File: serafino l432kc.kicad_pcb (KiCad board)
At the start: 4 copper layers, 17.8 x 35.6 mm, 31 parts, among them J1 USB_B_Micro, J2 Conn_01x14, J3 Conn_01x14, Q1 AO3401A, SW1 SW_Push, U1 AP2112K-3.3, U2 USBLC6-2SC6, U3 STM32L432KCUx, Y1 32.768K

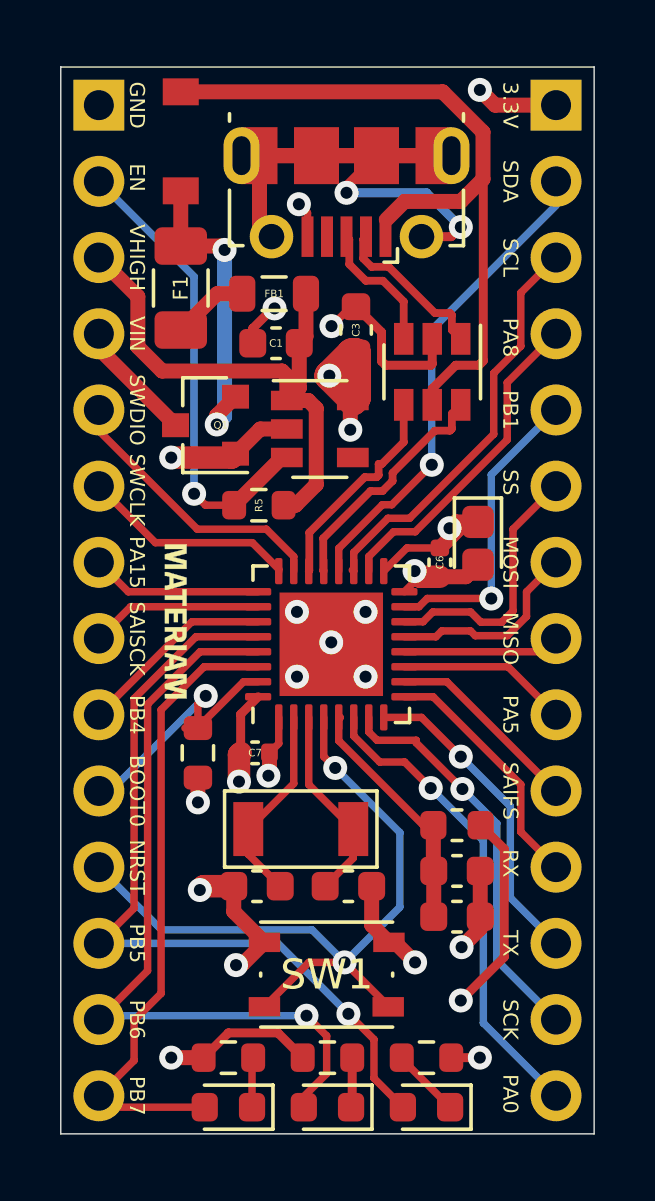
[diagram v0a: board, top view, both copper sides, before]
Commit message: Cambio de layout en leds
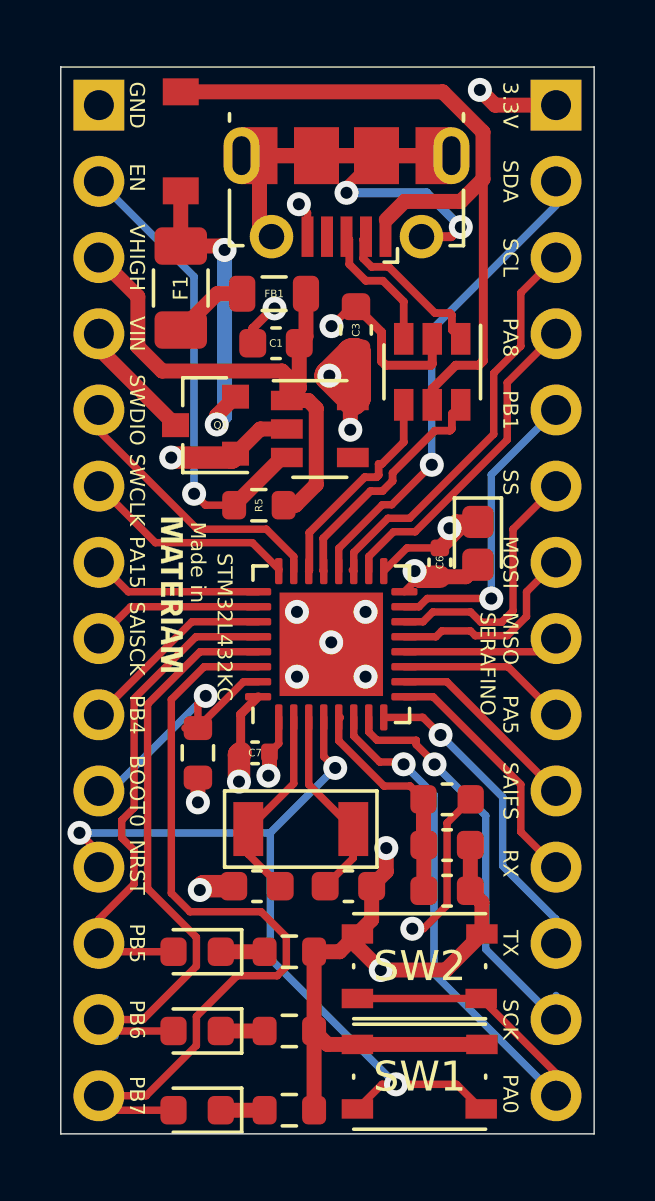
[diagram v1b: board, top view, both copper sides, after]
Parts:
- added SW2: SW_Push, Button_Switch_SMD:SW_Push_1P1T_NO_Vertical_Wuerth_434133025816, F.Cu at (199.4, 121.0)
- moved D1 9.24 mm to (192.0, 120.5)
- moved R1 5.78 mm to (195.1, 120.5)
- moved D3 5.03 mm to (192.0, 123.2)
- moved SW1 4.60 mm to (199.4, 124.7)
- moved R4 2.68 mm to (195.1, 125.8), turned to 0 degrees
- moved R3 1.55 mm to (195.1, 123.2), turned to 0 degrees
- moved D4 1.05 mm to (192.0, 125.8)
- moved C10 0.92 mm to (200.3, 117.0)
- moved C9 0.92 mm to (200.3, 118.5)
- moved L1 0.92 mm to (200.3, 115.5)
- moved G*** 0.90 mm to (191.1, 108.6)
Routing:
- net LED0: track 26.8 -> 16.5 mm, vias 1 -> 0
- net GND: track 36.3 -> 45.0 mm, vias 17 -> 14
- net PA0: track 15.9 -> 24.2 mm
- net LED2: track 21.2 -> 27.1 mm
- net LED1: track 26.3 -> 21.4 mm, vias 1 -> 0
- net NRST: track 24.9 -> 27.6 mm, vias 2 -> 3
- net +3V3: track 22.9 -> 21.5 mm
- net Net-(D1-Pad1): track 2.32 -> 1.46 mm
- net SPI1_SCK: track 13.4 -> 14.2 mm
- net +3.3VA: track 8.20 -> 7.52 mm
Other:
- board text added: "Made in"
- board text added: "SERAFINO"
- board text added: "STM32L432KC"

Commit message: BOM start
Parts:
- added G***: LOGO, serafino l432kc:cupid, F.Cu at (197.4, 104.8)
- moved G*** 0.07 mm to (191.2, 108.6)
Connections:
- R2 pad 1: +3V3 -> GND
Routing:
- net GND: track 45.0 -> 46.4 mm
- net +3V3: track 21.5 -> 20.7 mm, vias 7 -> 6
- net BOOT0: track 9.15 -> 8.51 mm
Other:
- board text added: "* Ultra-low-power * Arm ® Cortex ® M4 * 32-bit MCU+FPU@80Mhz * 256KB Flash * 64KB SRAM"
- board text added: "RST"
- board text added: "SERAFINO L432"
- board text added: "SW0"
- board text added: "http://materiam.com/serafino"
- board text removed: "SERAFINO"

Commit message: version acorde con primer prototipo
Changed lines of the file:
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@@
     (thickness 1.6)
     (drawings 41)
-    (tracks 374)
+    (tracks 377)
     (zones 0)
     (modules 33)
@@
   )
   (setup
-    (last_trace_width 0.25)
+    (last_trace_width 0.3)
     (user_trace_width 0.3)
     (user_trace_width 0.5)
@@
   (segment (start 200.6444 124.968) (end 201.4654 125.789) (width 0.25) (layer F.Cu) (net 3) (status 20))
   (segment (start 198.628 124.968) (end 200.6444 124.968) (width 0.25) (layer F.Cu) (net 3))
-  (segment (start 198.992 107.089) (end 200.0885 107.089) (width 0.25) (layer F.Cu) (net 4) (status 20))
-  (segment (start 198.219 107.862) (end 198.992 107.089) (width 0.25) (layer F.Cu) (net 4) (status 10))
   (segment (start 200.956 106.2215) (end 201.3585 106.2215) (width 0.5) (layer F.Cu) (net 4) (status 30))
   (segment (start 200.0885 107.089) (end 200.956 106.2215) (width 0.5) (layer F.Cu) (net 4) (status 30))
-  (segment (start 194.719 113.609) (end 194.409 113.919) (width 0.25) (layer F.Cu) (net 4) (status 20))
-  (segment (start 194.719 112.737) (end 194.719 113.609) (width 0.25) (layer F.Cu) (net 4) (status 10))
   (segment (start 197.188 100.7035) (end 197.2945 100.597) (width 0.5) (layer F.Cu) (net 4) (status 30))
   (segment (start 203.962 92.329) (end 203.454 92.329) (width 0.5) (layer F.Cu) (net 4) (status 30))
@@
   (segment (start 200.3298 118.994234) (end 199.541918 119.782116) (width 0.25) (layer F.Cu) (net 4))
   (segment (start 201.1173 115.4684) (end 200.3298 116.2559) (width 0.25) (layer F.Cu) (net 4) (status 10))
+  (segment (start 198.907304 107.089) (end 200.0885 107.089) (width 0.3) (layer F.Cu) (net 4))
+  (segment (start 198.219 107.777304) (end 198.907304 107.089) (width 0.3) (layer F.Cu) (net 4))
+  (segment (start 198.219 107.862) (end 198.219 107.777304) (width 0.3) (layer F.Cu) (net 4))
+  (segment (start 194.719 113.609) (end 194.409 113.919) (width 0.3) (layer F.Cu) (net 4))
+  (segment (start 194.719 112.737) (end 194.719 113.609) (width 0.3) (layer F.Cu) (net 4))
   (segment (start 195.219 114.943) (end 193.703 116.459) (width 0.25) (layer F.Cu) (net 5) (status 20))
   (segment (start 195.219 112.737) (end 195.219 114.943) (width 0.25) (layer F.Cu) (net 5) (status 10))
@@
   (segment (start 202.184 117.690002) (end 203.962 119.468002) (width 0.25) (layer B.Cu) (net 22) (status 20))
   (segment (start 202.184 115.395304) (end 202.184 117.690002) (width 0.25) (layer B.Cu) (net 22))
-  (segment (start 197.995988 113.49951) (end 199.30149 113.49951) (width 0.25) (layer F.Cu) (net 23))
-  (segment (start 197.719 113.222522) (end 197.995988 113.49951) (width 0.25) (layer F.Cu) (net 23))
   (segment (start 197.719 112.737) (end 197.719 113.222522) (width 0.25) (layer F.Cu) (net 23) (status 10))
   (via (at 199.911198 114.303214) (size 0.8) (drill 0.4) (layers F.Cu B.Cu) (net 23))
   (segment (start 199.883882 114.22888) (end 199.91578 114.22888) (width 0.25) (layer F.Cu) (net 23))
-  (segment (start 199.30149 113.646488) (end 199.883882 114.22888) (width 0.25) (layer F.Cu) (net 23))
-  (segment (start 199.30149 113.49951) (end 199.30149 113.646488) (width 0.25) (layer F.Cu) (net 23))
   (segment (start 203.962 122.008002) (end 203.962 122.809) (width 0.25) (layer B.Cu) (net 23) (status 30))
   (segment (start 201.618009 120.465009) (end 203.962 122.809) (width 0.25) (layer B.Cu) (net 23) (status 20))
   (segment (start 201.618009 116.010025) (end 201.618009 120.465009) (width 0.25) (layer B.Cu) (net 23))
   (segment (start 199.911198 114.303214) (end 201.618009 116.010025) (width 0.25) (layer B.Cu) (net 23))
+  (segment (start 199.182983 113.574999) (end 199.911198 114.303214) (width 0.25) (layer F.Cu) (net 23))
+  (segment (start 198.071477 113.574999) (end 199.182983 113.574999) (width 0.25) (layer F.Cu) (net 23))
+  (segment (start 197.76899 113.272512) (end 198.071477 113.574999) (width 0.25) (layer F.Cu) (net 23))
+  (segment (start 197.757478 113.222522) (end 197.76899 113.234034) (width 0.25) (layer F.Cu) (net 23))
+  (segment (start 197.76899 113.234034) (end 197.76899 113.272512) (width 0.25) (layer F.Cu) (net 23))
+  (segment (start 197.719 113.222522) (end 197.757478 113.222522) (width 0.25) (layer F.Cu) (net 23))
   (segment (start 197.219 113.358932) (end 198.084578 114.22451) (width 0.25) (layer F.Cu) (net 24))
   (segment (start 197.219 112.737) (end 197.219 113.358932) (width 0.25) (layer F.Cu) (net 24) (status 10))

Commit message: My name is Seraph
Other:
- board text added: "3.3v"
- board text added: "L432"
- board text added: "SERAPH"
- board text removed: "SERAFINO L432"

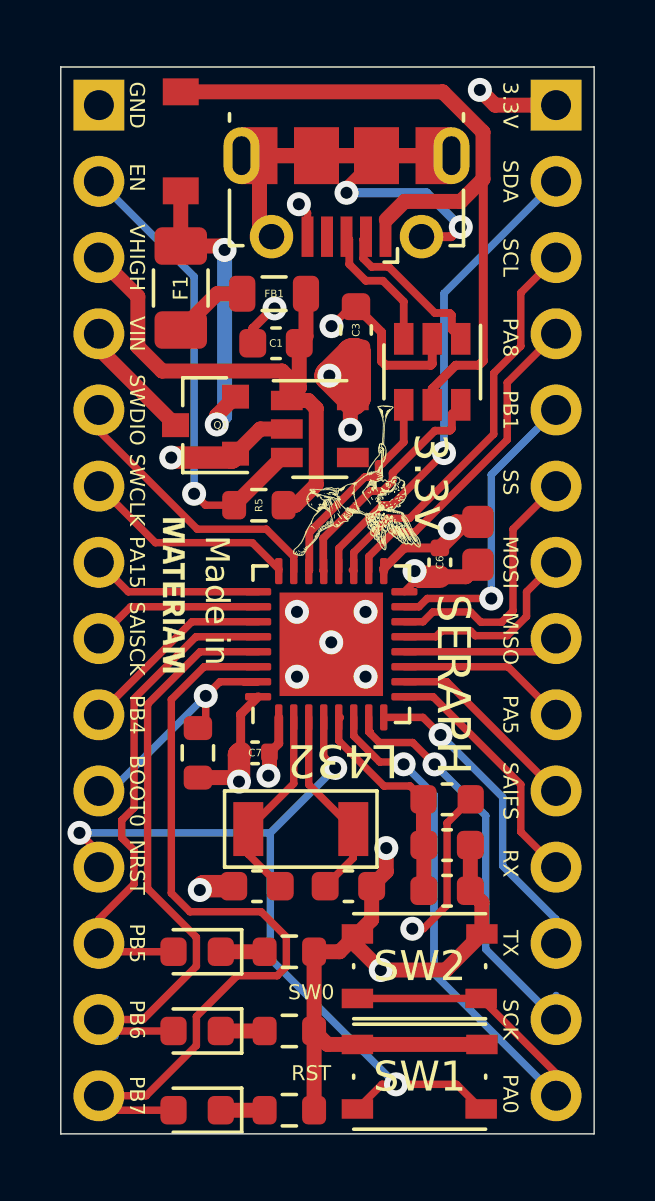
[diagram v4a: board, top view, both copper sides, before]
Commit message: PWM Leds
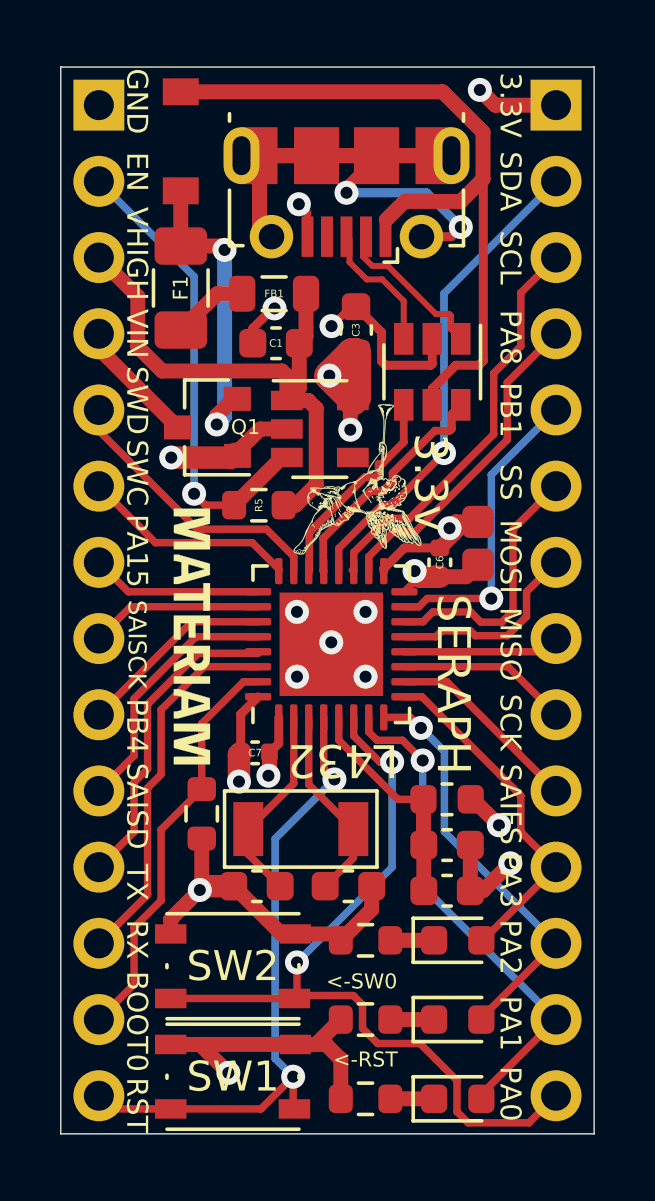
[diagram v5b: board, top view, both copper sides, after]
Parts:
- added G***: LOGO, serafino l432kc:big_cupid, B.Cu at (194.9, 103.4)
- FB1: value 600@600MHz -> 600@100MHz
- L1: value 39h -> 600@100MHz
- Q1: value AO3401A -> SI3401A-TP
- R1, R3, R4: value 1.5K -> 1K
- moved D4 10.4 mm to (200.7, 120.2), turned to 0 degrees
- moved D1 9.97 mm to (200.7, 125.5), turned to 0 degrees
- moved D3 8.70 mm to (200.7, 122.8), turned to 0 degrees
- moved SW1 6.22 mm to (193.2, 124.7)
- moved SW2 6.22 mm to (193.2, 121.0)
- moved R4 6.21 mm to (197.6, 120.2), turned to 180 degrees
- moved R1 5.52 mm to (197.6, 125.5), turned to 180 degrees
- moved R3 2.57 mm to (197.6, 122.8), turned to 180 degrees
- moved R2 2.04 mm to (192.2, 116.0)
- moved G*** 1.58 mm to (191.8, 110.0)
- moved Q1 0.10 mm to (192.3, 103.1)
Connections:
- J2 pad 10: BOOT0 -> SAI1_SD_B
- J2 pad 11: NRST -> USART1_TX
- J2 pad 12: LED0 -> USART1_RX
- J2 pad 13: LED1 -> BOOT0
- J2 pad 14: LED2 -> NRST
- J3 pad 11: USART2_RX -> LED2
- J3 pad 12: USART2_TX -> LED1
- J3 pad 13: SPI1_SCK -> LED0
- J3 pad 9: PA5 -> SPI1_SCK
- U3 pad 11: PA5 -> SPI1_SCK
- U3 pad 28: LED0 -> SAI1_SD_B
- U3 pad 29: LED1 -> USART1_TX
- U3 pad 30: LED2 -> USART1_RX
- U3 pad 7: SPI1_SCK -> LED0
- U3 pad 8: USART2_TX -> LED1
- U3 pad 9: USART2_RX -> LED2
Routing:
- net LED2: track 27.1 -> 11.6 mm
- net USART1_RX: track 0.00 -> 12.5 mm
- net USART2_TX: track 10.7 -> 0.00 mm, vias 1 -> 0
- net USART1_TX: track 0.00 -> 10.5 mm
- net SAI1_SD_B: track 0.00 -> 8.55 mm
- net SPI1_SCK: track 14.2 -> 5.72 mm, vias 1 -> 0
- net USART2_RX: track 8.33 -> 0.00 mm
- net LED1: track 21.4 -> 14.0 mm, vias 0 -> 1
- net NRST: track 27.6 -> 21.4 mm, vias 3 -> 2
- net PA5: track 5.72 -> 0.00 mm
- net BOOT0: track 8.51 -> 13.7 mm, vias 1 -> 0
- net +3V3: track 20.7 -> 16.7 mm
- net PA0: track 24.2 -> 27.6 mm, vias 1 -> 2
- net GND: track 46.4 -> 45.4 mm
- net LED0: track 16.5 -> 16.8 mm, vias 0 -> 1
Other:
- board text added: "* STM32L432KC * Ultra-low-power * Arm ® Cortex ® M4 * 32-bit MCU+FPU@80Mhz * 256KB Flash * 64KB SRAM"
- board text added: "<-RST"
- board text added: "<-SW0"
- board text added: "PA1"
- board text added: "PA2"
- board text added: "PA3"
- board text added: "SAISD"
- board text added: "SERAPH L4"
- board text added: "SWC"
- board text added: "SWD"
- board text added: "http://materiam.com/seraph"
- board text removed: "* Ultra-low-power * Arm ® Cortex ® M4 * 32-bit MCU+FPU@80Mhz * 256KB Flash * 64KB SRAM"
- board text removed: "Made in"
- board text removed: "NRST"
- board text removed: "PA5"
- board text removed: "PB5"
- board text removed: "PB6"
- board text removed: "PB7"
- board text removed: "STM32L432KC"
- board text removed: "SW0"
- board text removed: "SWCLK"
- board text removed: "SWDIO"
- board text removed: "http://materiam.com/serafino"

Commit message: BOOT0 a SW0
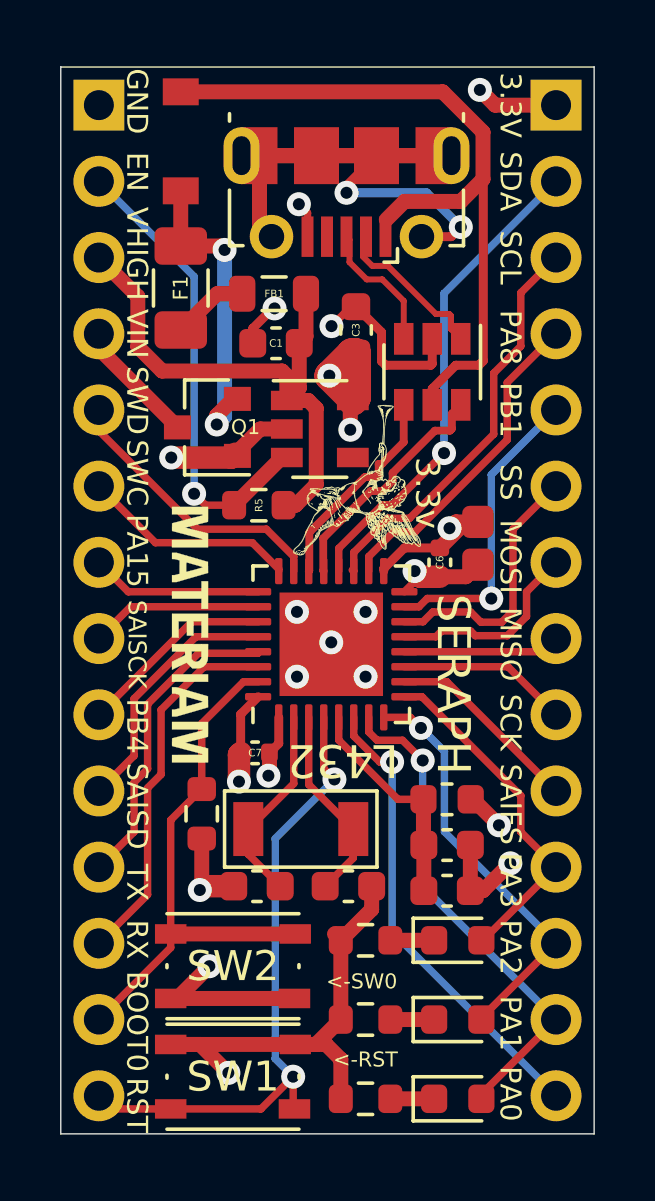
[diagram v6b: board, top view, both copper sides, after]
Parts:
- moved G*** 2.72 mm to (195.3, 100.7)
- moved G*** 0.09 mm to (191.8, 110.0)
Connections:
- SW2 pad 1: GND -> BOOT0
- SW2 pad 2: PA0 -> +3V3
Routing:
- net PA0: track 27.6 -> 15.6 mm, vias 2 -> 1
- net +3V3: track 16.7 -> 22.5 mm, vias 6 -> 7
- net BOOT0: track 13.7 -> 17.9 mm
- net GND: track 45.4 -> 42.2 mm
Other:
- board text added: "* STM32L432KC Arm Cortex M4 * 64KB SRAM/256KB Flash/80Mhz * * 32-bit MCU+FPU@80Mhz * 256KB Flash *"
- board text removed: "* STM32L432KC * Ultra-low-power * Arm ® Cortex ® M4 * 32-bit MCU+FPU@80Mhz * 256KB Flash * 64KB SRAM"

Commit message: Silk screen updated
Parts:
- moved G*** 3.86 mm to (197.9, 97.8)
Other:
- board text added: "* STM32L432KC ARM Cortex M4 * 64KB SRAM/256KB Flash/80Mhz * Embedded USB DFU Bootloader Press RESET while holding BOOT0 to enter DFU mode."
- board text removed: "* STM32L432KC Arm Cortex M4 * 64KB SRAM/256KB Flash/80Mhz * * 32-bit MCU+FPU@80Mhz * 256KB Flash *"

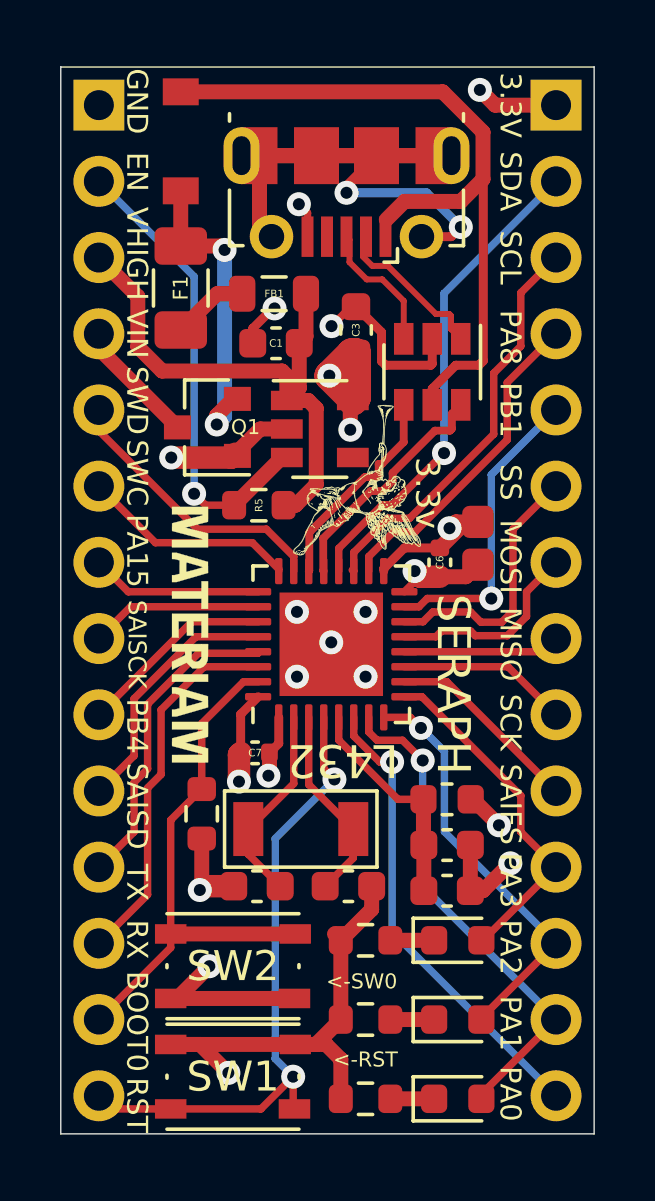
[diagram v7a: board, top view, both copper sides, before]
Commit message: DFU LED Indicator (PA6/MISO)
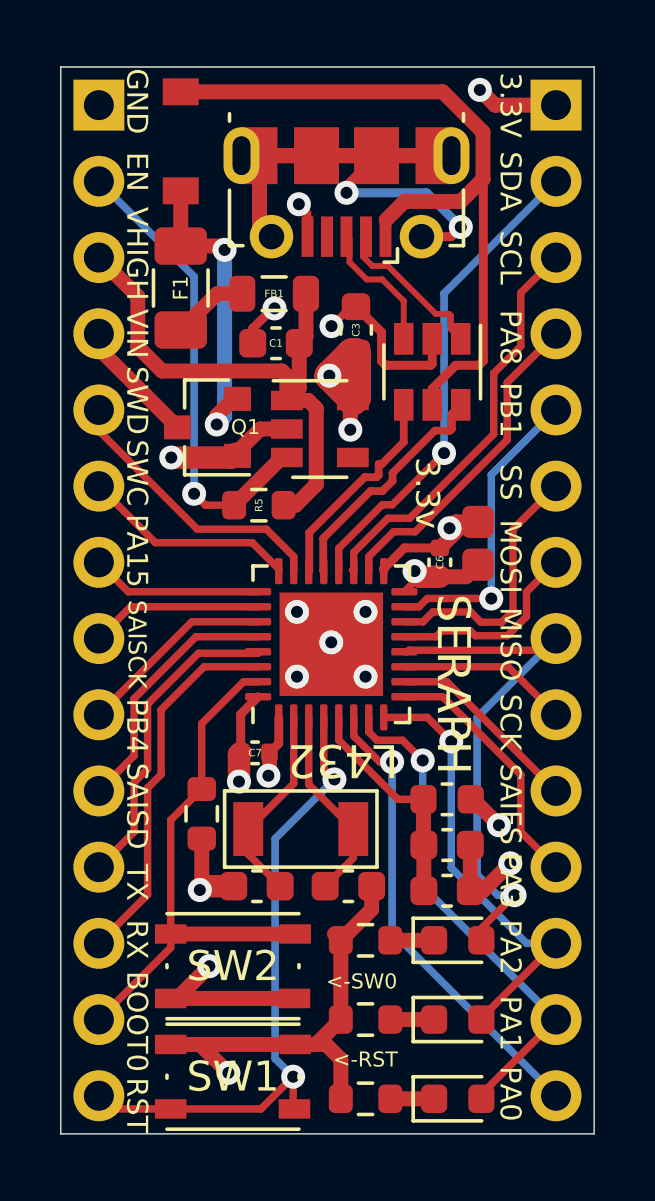
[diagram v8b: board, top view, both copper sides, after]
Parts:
- removed G***: LOGO, serafino l432kc:big_cupid
- removed G***: LOGO, serafino l432kc:cupid
- removed G***: LOGO, serafino l432kc:logo_materiam
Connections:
- D4 pad 2: LED2 -> SPI1_MISO
- J3 pad 11: LED2 -> PA3
- U3 pad 9: LED2 -> PA3
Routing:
- net SPI1_MISO: track 5.24 -> 17.7 mm, vias 0 -> 1
- net LED2: track 11.6 -> 0.00 mm
- net PA3: track 0.00 -> 8.52 mm
- net LED1: track 14.0 -> 14.9 mm
